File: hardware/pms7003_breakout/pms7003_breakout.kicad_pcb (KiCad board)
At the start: 2 copper layers, 16.5 x 25.4 mm, 3 parts, among them J1 PMS7003, J2 Header

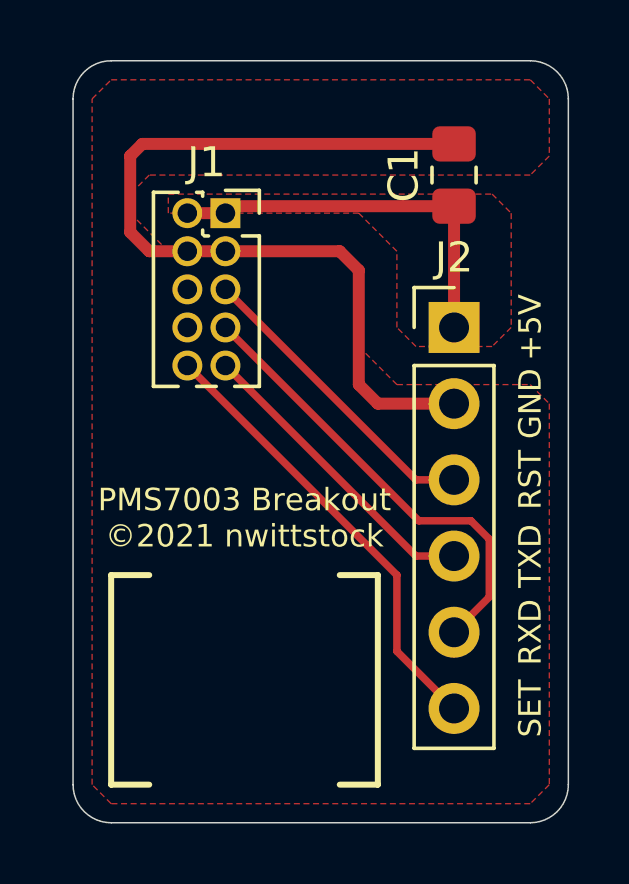
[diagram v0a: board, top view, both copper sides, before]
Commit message: add version to silkscreen
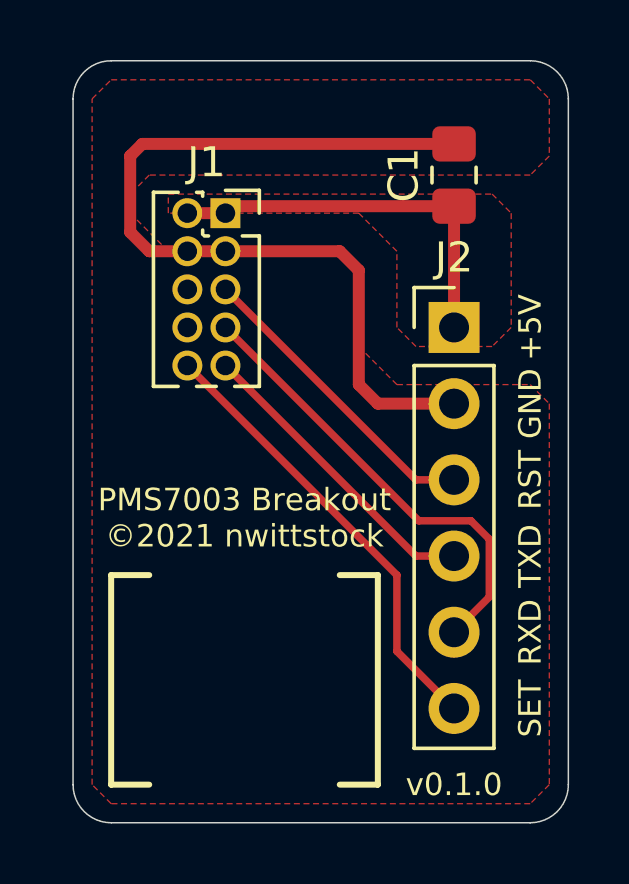
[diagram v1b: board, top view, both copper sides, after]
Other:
- board text added: "v0.1.0"
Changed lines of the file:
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@@
   (general
     (thickness 1.6)
-    (drawings 21)
+    (drawings 22)
     (tracks 27)
     (zones 0)
@@
     (pad_to_mask_clearance 0)
     (aux_axis_origin 0 0)
-    (visible_elements FFFFFF7F)
+    (visible_elements 7FFFFFFF)
     (pcbplotparams
       (layerselection 0x010fc_ffffffff)
@@
       (effects (font (size 1 1) (thickness 0.15)))
     )
+    (fp_line (start 1.4875 -0.635) (end -1.07 -0.635) (layer F.Fab) (width 0.1))
+    (fp_line (start -1.07 -0.635) (end -1.07 5.715) (layer F.Fab) (width 0.1))
+    (fp_line (start -1.07 5.715) (end 2.34 5.715) (layer F.Fab) (width 0.1))
+    (fp_line (start 2.34 5.715) (end 2.34 0.2175) (layer F.Fab) (width 0.1))
+    (fp_line (start 2.34 0.2175) (end 1.4875 -0.635) (layer F.Fab) (width 0.1))
+    (fp_line (start 2.4 5.775) (end 1.57753 5.775) (layer F.SilkS) (width 0.12))
+    (fp_line (start -0.30753 5.775) (end -1.13 5.775) (layer F.SilkS) (width 0.12))
+    (fp_line (start 0.96247 5.775) (end 0.30753 5.775) (layer F.SilkS) (width 0.12))
+    (fp_line (start 2.4 0.76) (end 2.4 5.775) (layer F.SilkS) (width 0.12))
+    (fp_line (start -1.13 -0.695) (end -1.13 5.775) (layer F.SilkS) (width 0.12))
+    (fp_line (start 2.4 0.76) (end 1.833471 0.76) (layer F.SilkS) (width 0.12))
+    (fp_line (start 0.706529 0.76) (end 0.563471 0.76) (layer F.SilkS) (width 0.12))
+    (fp_line (start 0.51 0.706529) (end 0.51 0.563471) (layer F.SilkS) (width 0.12))
+    (fp_line (start 0.51 -0.563471) (end 0.51 -0.695) (layer F.SilkS) (width 0.12))
+    (fp_line (start 0.51 -0.695) (end 0.30753 -0.695) (layer F.SilkS) (width 0.12))
+    (fp_line (start -0.30753 -0.695) (end -1.13 -0.695) (layer F.SilkS) (width 0.12))
+    (fp_line (start 2.4 0) (end 2.4 -0.76) (layer F.SilkS) (width 0.12))
+    (fp_line (start 2.4 -0.76) (end 1.27 -0.76) (layer F.SilkS) (width 0.12))
+    (fp_line (start -1.6 -1.15) (end -1.6 6.25) (layer F.CrtYd) (width 0.05))
+    (fp_line (start -1.6 6.25) (end 2.85 6.25) (layer F.CrtYd) (width 0.05))
+    (fp_line (start 2.85 6.25) (end 2.85 -1.15) (layer F.CrtYd) (width 0.05))
     (fp_line (start 2.85 -1.15) (end -1.6 -1.15) (layer F.CrtYd) (width 0.05))
-    (fp_line (start 2.85 6.25) (end 2.85 -1.15) (layer F.CrtYd) (width 0.05))
-    (fp_line (start -1.6 6.25) (end 2.85 6.25) (layer F.CrtYd) (width 0.05))
-    (fp_line (start -1.6 -1.15) (end -1.6 6.25) (layer F.CrtYd) (width 0.05))
-    (fp_line (start 2.4 -0.76) (end 1.27 -0.76) (layer F.SilkS) (width 0.12))
-    (fp_line (start 2.4 0) (end 2.4 -0.76) (layer F.SilkS) (width 0.12))
-    (fp_line (start -0.30753 -0.695) (end -1.13 -0.695) (layer F.SilkS) (width 0.12))
-    (fp_line (start 0.51 -0.695) (end 0.30753 -0.695) (layer F.SilkS) (width 0.12))
-    (fp_line (start 0.51 -0.563471) (end 0.51 -0.695) (layer F.SilkS) (width 0.12))
-    (fp_line (start 0.51 0.706529) (end 0.51 0.563471) (layer F.SilkS) (width 0.12))
-    (fp_line (start 0.706529 0.76) (end 0.563471 0.76) (layer F.SilkS) (width 0.12))
-    (fp_line (start 2.4 0.76) (end 1.833471 0.76) (layer F.SilkS) (width 0.12))
-    (fp_line (start -1.13 -0.695) (end -1.13 5.775) (layer F.SilkS) (width 0.12))
-    (fp_line (start 2.4 0.76) (end 2.4 5.775) (layer F.SilkS) (width 0.12))
-    (fp_line (start 0.96247 5.775) (end 0.30753 5.775) (layer F.SilkS) (width 0.12))
-    (fp_line (start -0.30753 5.775) (end -1.13 5.775) (layer F.SilkS) (width 0.12))
-    (fp_line (start 2.4 5.775) (end 1.57753 5.775) (layer F.SilkS) (width 0.12))
-    (fp_line (start 2.34 0.2175) (end 1.4875 -0.635) (layer F.Fab) (width 0.1))
-    (fp_line (start 2.34 5.715) (end 2.34 0.2175) (layer F.Fab) (width 0.1))
-    (fp_line (start -1.07 5.715) (end 2.34 5.715) (layer F.Fab) (width 0.1))
-    (fp_line (start -1.07 -0.635) (end -1.07 5.715) (layer F.Fab) (width 0.1))
-    (fp_line (start 1.4875 -0.635) (end -1.07 -0.635) (layer F.Fab) (width 0.1))
     (fp_text user %R (at 0.635 2.54 180) (layer F.Fab)
       (effects (font (size 1 1) (thickness 0.15)))
@@
       (effects (font (size 1 1) (thickness 0.15)))
     )
+    (fp_line (start 1.88 0.98) (end -1.88 0.98) (layer F.CrtYd) (width 0.05))
+    (fp_line (start 1.88 -0.98) (end 1.88 0.98) (layer F.CrtYd) (width 0.05))
+    (fp_line (start -1.88 -0.98) (end 1.88 -0.98) (layer F.CrtYd) (width 0.05))
+    (fp_line (start -1.88 0.98) (end -1.88 -0.98) (layer F.CrtYd) (width 0.05))
+    (fp_line (start -0.261252 0.735) (end 0.261252 0.735) (layer F.SilkS) (width 0.12))
+    (fp_line (start -0.261252 -0.735) (end 0.261252 -0.735) (layer F.SilkS) (width 0.12))
+    (fp_line (start 1 0.625) (end -1 0.625) (layer F.Fab) (width 0.1))
+    (fp_line (start 1 -0.625) (end 1 0.625) (layer F.Fab) (width 0.1))
+    (fp_line (start -1 -0.625) (end 1 -0.625) (layer F.Fab) (width 0.1))
+    (fp_line (start -1 0.625) (end -1 -0.625) (layer F.Fab) (width 0.1))
     (fp_text user %R (at 0 0 90) (layer F.Fab)
       (effects (font (size 0.5 0.5) (thickness 0.08)))
     )
-    (fp_line (start -1 0.625) (end -1 -0.625) (layer F.Fab) (width 0.1))
-    (fp_line (start -1 -0.625) (end 1 -0.625) (layer F.Fab) (width 0.1))
-    (fp_line (start 1 -0.625) (end 1 0.625) (layer F.Fab) (width 0.1))
-    (fp_line (start 1 0.625) (end -1 0.625) (layer F.Fab) (width 0.1))
-    (fp_line (start -0.261252 -0.735) (end 0.261252 -0.735) (layer F.SilkS) (width 0.12))
-    (fp_line (start -0.261252 0.735) (end 0.261252 0.735) (layer F.SilkS) (width 0.12))
-    (fp_line (start -1.88 0.98) (end -1.88 -0.98) (layer F.CrtYd) (width 0.05))
-    (fp_line (start -1.88 -0.98) (end 1.88 -0.98) (layer F.CrtYd) (width 0.05))
-    (fp_line (start 1.88 -0.98) (end 1.88 0.98) (layer F.CrtYd) (width 0.05))
-    (fp_line (start 1.88 0.98) (end -1.88 0.98) (layer F.CrtYd) (width 0.05))
     (pad 2 smd roundrect (at 1.0375 0 90) (size 1.175 1.45) (layers F.Cu F.Paste F.Mask) (roundrect_rratio 0.212766)
       (net 2 GND))
@@
       (effects (font (size 1 1) (thickness 0.15)))
     )
+    (fp_line (start -0.635 -1.27) (end 1.27 -1.27) (layer F.Fab) (width 0.1))
+    (fp_line (start 1.27 -1.27) (end 1.27 13.97) (layer F.Fab) (width 0.1))
+    (fp_line (start 1.27 13.97) (end -1.27 13.97) (layer F.Fab) (width 0.1))
+    (fp_line (start -1.27 13.97) (end -1.27 -0.635) (layer F.Fab) (width 0.1))
+    (fp_line (start -1.27 -0.635) (end -0.635 -1.27) (layer F.Fab) (width 0.1))
+    (fp_line (start -1.33 14.03) (end 1.33 14.03) (layer F.SilkS) (width 0.12))
+    (fp_line (start -1.33 1.27) (end -1.33 14.03) (layer F.SilkS) (width 0.12))
+    (fp_line (start 1.33 1.27) (end 1.33 14.03) (layer F.SilkS) (width 0.12))
+    (fp_line (start -1.33 1.27) (end 1.33 1.27) (layer F.SilkS) (width 0.12))
+    (fp_line (start -1.33 0) (end -1.33 -1.33) (layer F.SilkS) (width 0.12))
+    (fp_line (start -1.33 -1.33) (end 0 -1.33) (layer F.SilkS) (width 0.12))
+    (fp_line (start -1.8 -1.8) (end -1.8 14.5) (layer F.CrtYd) (width 0.05))
+    (fp_line (start -1.8 14.5) (end 1.8 14.5) (layer F.CrtYd) (width 0.05))
+    (fp_line (start 1.8 14.5) (end 1.8 -1.8) (layer F.CrtYd) (width 0.05))
     (fp_line (start 1.8 -1.8) (end -1.8 -1.8) (layer F.CrtYd) (width 0.05))
-    (fp_line (start 1.8 14.5) (end 1.8 -1.8) (layer F.CrtYd) (width 0.05))
-    (fp_line (start -1.8 14.5) (end 1.8 14.5) (layer F.CrtYd) (width 0.05))
-    (fp_line (start -1.8 -1.8) (end -1.8 14.5) (layer F.CrtYd) (width 0.05))
-    (fp_line (start -1.33 -1.33) (end 0 -1.33) (layer F.SilkS) (width 0.12))
-    (fp_line (start -1.33 0) (end -1.33 -1.33) (layer F.SilkS) (width 0.12))
-    (fp_line (start -1.33 1.27) (end 1.33 1.27) (layer F.SilkS) (width 0.12))
-    (fp_line (start 1.33 1.27) (end 1.33 14.03) (layer F.SilkS) (width 0.12))
-    (fp_line (start -1.33 1.27) (end -1.33 14.03) (layer F.SilkS) (width 0.12))
-    (fp_line (start -1.33 14.03) (end 1.33 14.03) (layer F.SilkS) (width 0.12))
-    (fp_line (start -1.27 -0.635) (end -0.635 -1.27) (layer F.Fab) (width 0.1))
-    (fp_line (start -1.27 13.97) (end -1.27 -0.635) (layer F.Fab) (width 0.1))
-    (fp_line (start 1.27 13.97) (end -1.27 13.97) (layer F.Fab) (width 0.1))
-    (fp_line (start 1.27 -1.27) (end 1.27 13.97) (layer F.Fab) (width 0.1))
-    (fp_line (start -0.635 -1.27) (end 1.27 -1.27) (layer F.Fab) (width 0.1))
     (fp_text user %R (at 0 6.35 90) (layer F.Fab)
       (effects (font (size 1 1) (thickness 0.15)))
@@
     )
   )
+  (gr_text v0.1.0 (at 142.24 124.46) (layer F.SilkS)
+    (effects (font (size 0.75 0.75) (thickness 0.15)))
+  )
   (gr_text "PMS7003 Breakout\n©2021 nwittstock\n" (at 135.255 115.57) (layer F.SilkS)
